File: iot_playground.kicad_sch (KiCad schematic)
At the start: 34 parts, among them J101 Micro_SD_Card_Det_Hirose_DM3C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, J102 Conn_01x02, J104 Conn_01x04, J105 Conn_01x04, J701 Conn_01x08, SW101 SW_SPST, SW102 SW_SPST, U101 ESP32-WROOM-32D, U102 LTR-F216A, U103 UHE4913, U104 LIS2DW12

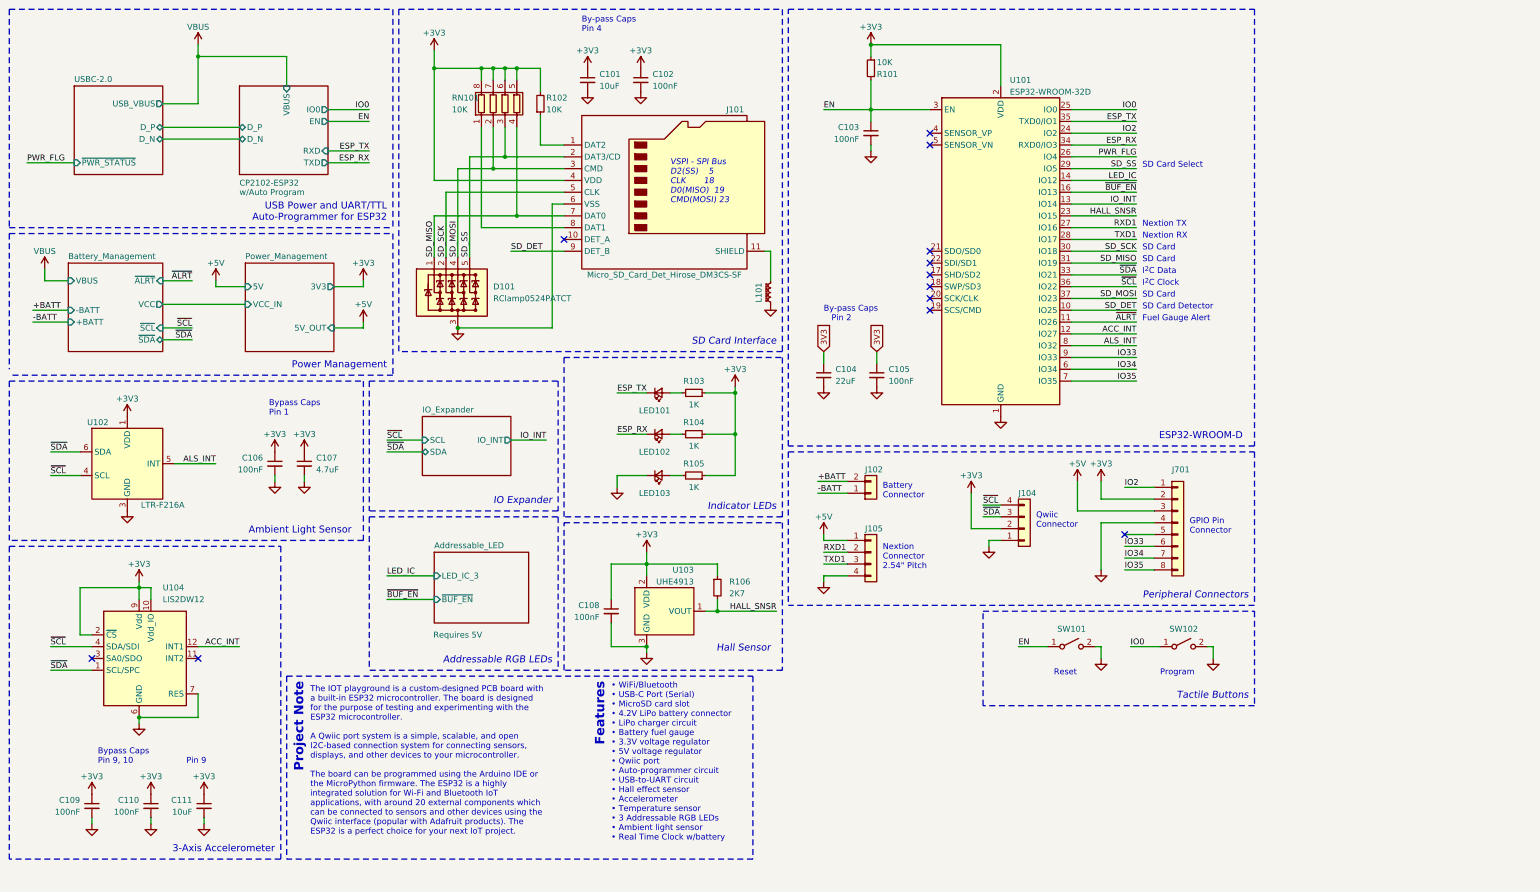
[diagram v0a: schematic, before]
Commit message: add RTC, humidity and temp sensors
updated footprint paths
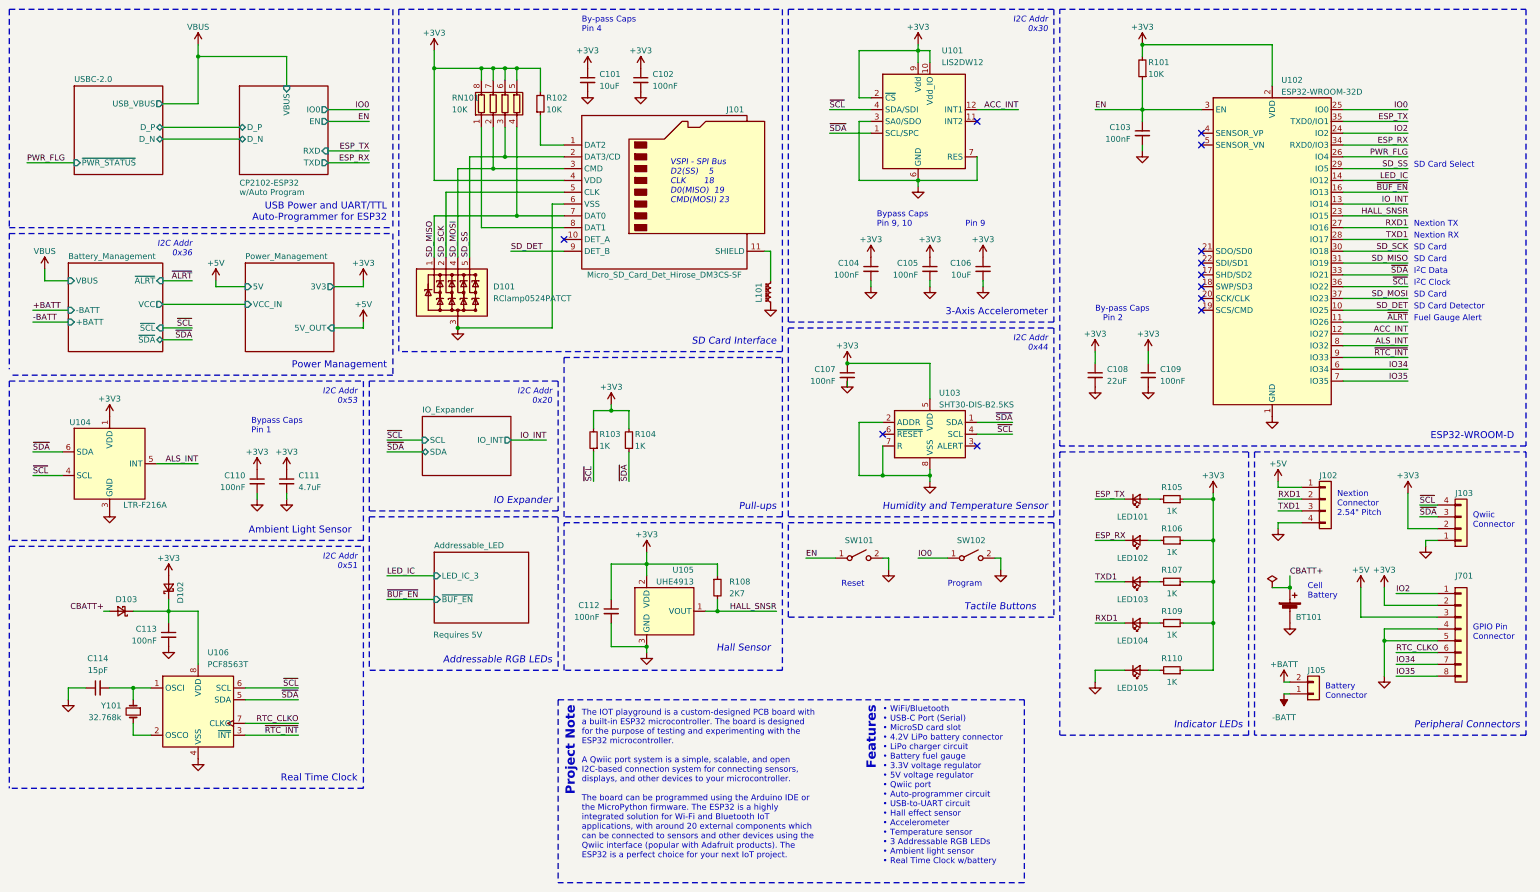
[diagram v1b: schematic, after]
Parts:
- added BT101: Battery_Cell, User Custom Footprint:BatteryHolder_CR1220, symbol Device:Battery_Cell
- added C107: 100nF, Capacitor_SMD:C_0603_1608Metric, symbol Device:C_Small
- added C113: 100nF, Capacitor_SMD:C_0805_2012Metric, symbol Device:C_Small
- added C114: 15pF, Capacitor_SMD:C_0603_1608Metric, symbol Device:C_Small
- added D102, D103: D_Schottky, Diode_SMD:D_SMA, symbol Device:D_Schottky_Small
- added LED103: BLUE, LED_SMD:LED_0603_1608Metric, symbol Device:LED_Small
- added LED104: GREEN, LED_SMD:LED_0603_1608Metric, symbol Device:LED_Small
- added R103, R104, R107, R109: 1K, Resistor_SMD:R_0603_1608Metric, symbol Device:R_Small
- added U103: SHT30-DIS-B2.5KS, Sensor_Humidity:Sensirion_DFN-8-1EP_2.5x2.5mm_P0.5mm_EP1.1x1.7mm, symbol Sensor_Humidity:SHT30-DIS
- added U106: PCF8563T, Package_SO:SOIC-8_3.9x4.9mm_P1.27mm, symbol Timer_RTC:PCF8563T
- added Y101: 32.768k, Crystal:Crystal_SMD_3215-2Pin_3.2x1.5mm, symbol Device:Crystal_Small
- renumbered C109 to C104, C110 to C105, C111 to C106, C104 to C108, C105 to C109, C106 to C110, C107 to C111, C108 to C112, J105 to J102, J104 to J103, J102 to J105, LED103 to LED105, R103 to R105, R104 to R106, R106 to R108, R105 to R110, U104 to U101, U101 to U102, U102 to U104, U103 to U105
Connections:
- net 3V3 is gone; now on net +3V3: C108.1, C109.1
- net +3V3: now also R101.2, C107.1, D102.2 (A), R103.2, R104.2, R107.1, R109.1, U103.5 (VDD); no longer R101.1
- net EN: now also R101.1; no longer R101.2
- net GND: now also J701.5 (Pin_5), U101.3 (SA0/SDO), BT101.2 (-), C107.2, C113.2, C114.1, U103.2 (ADDR), U103.7 (R), U103.8 (VSS), U103.9 (VSS), U106.4 (VSS)
- net RXD1: now also LED104.1 (K)
- net TXD1: now also LED103.1 (K)
- net ~{SCL}: now also R103.1, U103.4 (SCL), U106.6 (SCL)
- net ~{SDA}: now also R104.1, U103.1 (SDA), U106.5 (SDA)
- net IO33 renamed RTC_CLKO
- net RTC_CLKO: now also U106.7 (CLKO); no longer U102.9 (IO33)
- new net: C113.1, D102.1 (K), D103.1 (K), U106.8 (VDD)
- new net: C114.2, U106.1 (OSCI), Y101.1
- new net: U106.2 (OSCO), Y101.2
- new net: LED103.2 (A), R107.2
- new net: LED104.2 (A), R109.2
- new net CBATT+: BT101.1 (+), D103.2 (A)
- new net ~{RTC_INT}: U102.9 (IO33), U106.3 (~{INT})
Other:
- note added: "Cell Battery"
- note added: "Humidity and Temperature Sensor"
- note added: "I2C Addr 0x20"
- note added: "I2C Addr 0x30"
- note added: "I2C Addr 0x36"
- note added: "I2C Addr 0x44"
- note added: "I2C Addr 0x51"
- note added: "I2C Addr 0x53"
- note added: "Pull-ups"
- note added: "Real Time Clock"
- moved on the sheet: C103, C104, C105, C106, C108, C109, C110, C111, J102, J103, J105, J701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

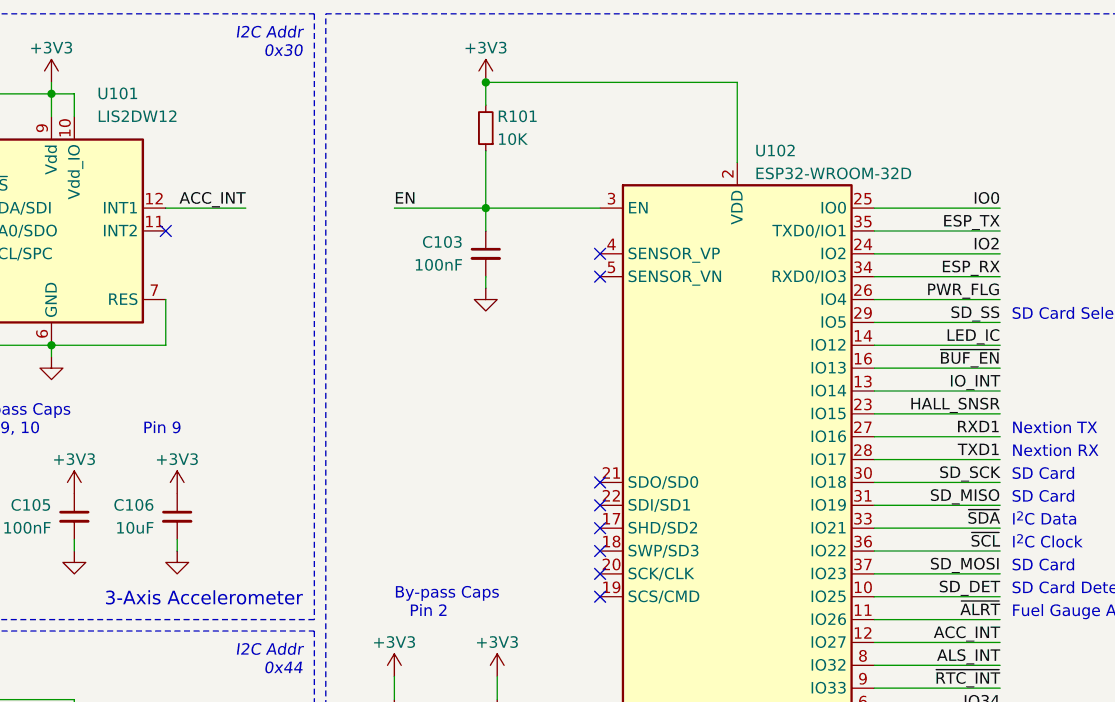
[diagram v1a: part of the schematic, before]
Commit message: update LCSC parts and footprints
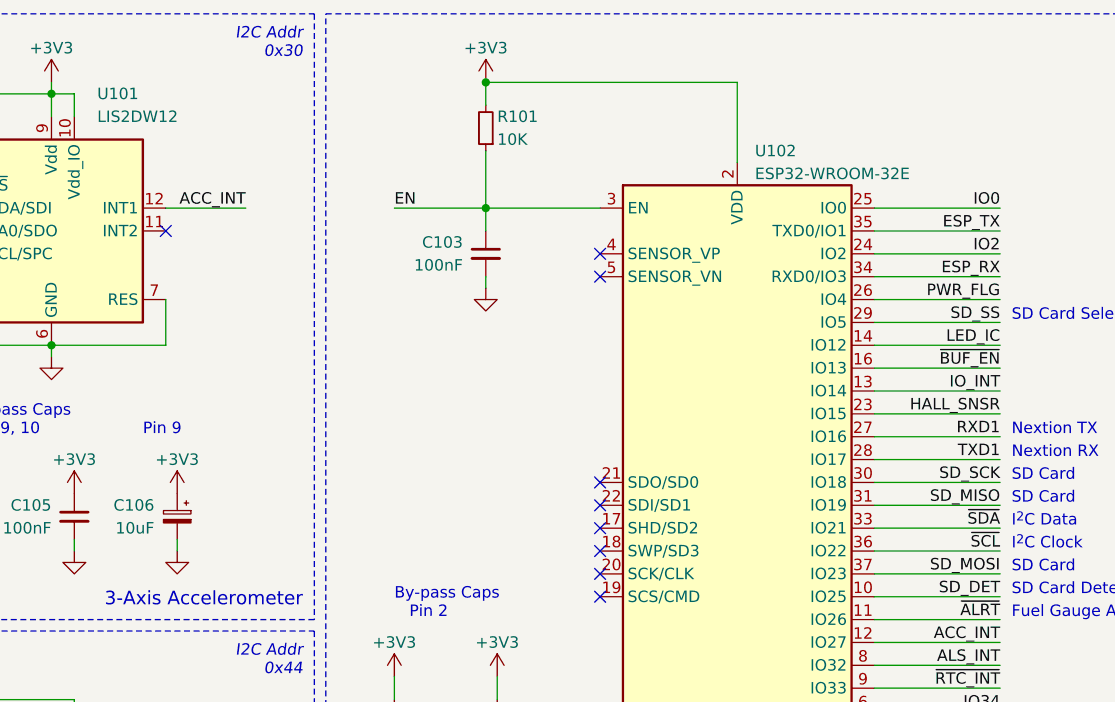
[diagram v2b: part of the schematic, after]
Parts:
- C106: footprint Capacitor_SMD:C_0603_1608Metric -> Capacitor_SMD:CP_Elec_5x5.4; symbol Device:C_Small -> Device:C_Polarized_Small; LCSC (none) -> C335978
- J102: footprint (none) -> Connector_PinHeader_2.54mm:PinHeader_1x04_P2.54mm_Vertical
- J103: footprint (none) -> Connector_JST:JST_SH_BM04B-SRSS-TB_1x04-1MP_P1.00mm_Vertical
- R103, R104: LCSC (none) -> C21190
- U102: value ESP32-WROOM-32D -> ESP32-WROOM-32E; LCSC (none) -> C701341
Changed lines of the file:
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@@
       (effects (font (size 1.27 1.27)) hide)
     )
-    (property "LCSC" "" (at 140.97 106.68 0)
+    (property "LCSC" "C21190" (at 140.97 106.68 0)
       (effects (font (size 1.27 1.27)) hide)
     )
@@
       (effects (font (size 1.27 1.27)) (justify left) hide)
     )
-    (property "Footprint" "" (at 327.66 125.73 0)
+    (property "Footprint" "Connector_JST:JST_SH_BM04B-SRSS-TB_1x04-1MP_P1.00mm_Vertical" (at 327.66 125.73 0)
       (effects (font (size 1.27 1.27)) hide)
     )
@@
       (effects (font (size 1.27 1.27)) (justify left) hide)
     )
-    (property "Footprint" "" (at 298.45 119.38 0)
+    (property "Footprint" "Connector_PinHeader_2.54mm:PinHeader_1x04_P2.54mm_Vertical" (at 298.45 119.38 0)
       (effects (font (size 1.27 1.27)) hide)
     )
@@
       (effects (font (size 1.27 1.27)) (justify left))
     )
-    (property "Value" "ESP32-WROOM-32D" (at 288.9759 31.75 0)
+    (property "Value" "ESP32-WROOM-32E" (at 288.9759 31.75 0)
       (effects (font (size 1.27 1.27)) (justify left))
     )
@@
     )
     (property "Datasheet" "https://www.espressif.com/sites/default/files/documentation/esp32-wroom-32d_esp32-wroom-32u_datasheet_en.pdf" (at 279.4 64.77 0)
+      (effects (font (size 1.27 1.27)) hide)
+    )
+    (property "LCSC" "C701341" (at 287.02 66.04 0)
       (effects (font (size 1.27 1.27)) hide)
     )
@@
       (effects (font (size 1.27 1.27)) hide)
     )
-    (property "LCSC" "" (at 148.59 106.68 0)
+    (property "LCSC" "C21190" (at 148.59 106.68 0)
       (effects (font (size 1.27 1.27)) hide)
     )
@@
     )
   )
-  (symbol (lib_id "Device:C_Small") (at 224.79 69.85 0) (mirror y) (unit 1)
+  (symbol (lib_id "Device:C_Polarized_Small") (at 224.79 69.85 0) (mirror y) (unit 1)
     (in_bom yes) (on_board yes) (dnp no)
     (property "Reference" "C106" (at 222.25 68.5862 0)
@@
       (effects (font (size 1.27 1.27)) (justify left))
     )
-    (property "Footprint" "Capacitor_SMD:C_0603_1608Metric" (at 224.79 69.85 0)
+    (property "Footprint" "Capacitor_SMD:CP_Elec_5x5.4" (at 224.79 69.85 0)
       (effects (font (size 1.27 1.27)) hide)
     )
@@
       (effects (font (size 1.27 1.27)) hide)
     )
-    (property "LCSC" "" (at 224.79 69.85 0)
-      (effects (font (size 1.27 1.27)) hide)
-    )
+    (property "LCSC" "C335978" (at 224.79 69.85 0)
+      (effects (font (size 1.27 1.27)) hide)
+    )

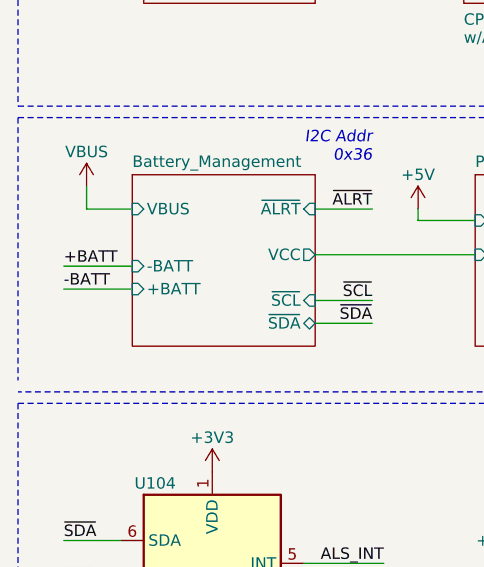
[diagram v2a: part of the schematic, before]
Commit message: update 3d models
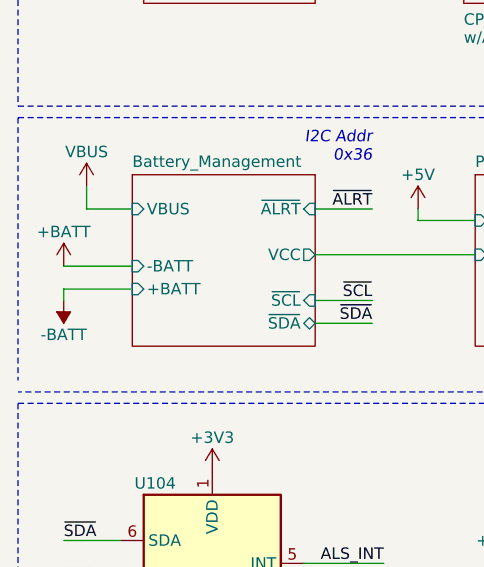
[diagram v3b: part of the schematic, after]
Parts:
- J103: footprint Connector_JST:JST_SH_BM04B-SRSS-TB_1x04-1MP_P1.00mm_Vertical -> Connector_JST:JST_SH_SM04B-SRSS-TB_1x04-1MP_P1.00mm_Horizontal
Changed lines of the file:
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@@
     (stroke (width 0) (type default))
   )
-  (wire (pts (xy 20.32 81.28) (xy 27.94 81.28))
-    (stroke (width 0) (type default))
-  )
   (wire (pts (xy 259.08 43.18) (xy 259.08 44.45))
     (stroke (width 0) (type default))
@@
     (stroke (width 0) (type default))
   )
+  (wire (pts (xy 20.32 81.28) (xy 27.94 81.28))
+    (stroke (width 0) (type default))
+  )
   (wire (pts (xy 311.15 142.24) (xy 322.58 142.24))
     (stroke (width 0) (type default))
@@
     (stroke (width 0) (type default))
   )
+  (wire (pts (xy 20.32 81.28) (xy 20.32 82.55))
+    (stroke (width 0) (type default))
+  )
   (wire (pts (xy 111.76 48.26) (xy 111.76 67.31))
     (stroke (width 0) (type default))
@@
     (effects (font (size 1.27 1.27)) (justify right bottom))
   )
-  (label "-BATT" (at 20.32 81.28 0) (fields_autoplaced)
-    (effects (font (size 1.27 1.27)) (justify left bottom))
-  )
   (label "TXD1" (at 316.23 63.5 180) (fields_autoplaced)
     (effects (font (size 1.27 1.27)) (justify right bottom))
@@
     (effects (font (size 1.27 1.27)) (justify left bottom))
   )
-  (label "+BATT" (at 20.32 78.74 0) (fields_autoplaced)
-    (effects (font (size 1.27 1.27)) (justify left bottom))
-  )
   (label "RTC_CLKO" (at 77.47 167.64 180) (fields_autoplaced)
     (effects (font (size 1.27 1.27)) (justify right bottom))
@@
       (effects (font (size 1.27 1.27)) (justify left) hide)
     )
-    (property "Footprint" "Connector_JST:JST_SH_BM04B-SRSS-TB_1x04-1MP_P1.00mm_Vertical" (at 327.66 125.73 0)
+    (property "Footprint" "Connector_JST:JST_SH_SM04B-SRSS-TB_1x04-1MP_P1.00mm_Horizontal" (at 327.66 125.73 0)
       (effects (font (size 1.27 1.27)) hide)
     )
@@
       (effects (font (size 1.27 1.27)) hide)
     )
+    (property "LCSC" "" (at 327.66 125.73 0)
+      (effects (font (size 1.27 1.27)) hide)
+    )
     (pin "1")
     (pin "2")
@@
     )
   )
+  (symbol (lib_id "power:-BATT") (at 20.32 82.55 180) (unit 1)
+    (in_bom yes) (on_board yes) (dnp no)
+    (property "Reference" "#PWR0159" (at 20.32 78.74 0)
+      (effects (font (size 1.27 1.27)) hide)
+    )
+    (property "Value" "-BATT" (at 20.32 86.36 0)
+      (effects (font (size 1.27 1.27)))
+    )
+    (property "Footprint" "" (at 20.32 82.55 0)
+      (effects (font (size 1.27 1.27)) hide)
+    )
+    (property "Datasheet" "" (at 20.32 82.55 0)
+      (effects (font (size 1.27 1.27)) hide)
+    )
+    (pin "1")
+    (instances
+      (project "iot_playground"
+        (path "/da21b043-c1be-47f1-86d6-d54e7594fd6d"
+          (reference "#PWR0159") (unit 1)
+        )
+      )
+    )
+  )
   (symbol (lib_id "power:+3V3") (at 210.82 21.59 0) (unit 1)
     (in_bom yes) (on_board yes) (dnp no)
@@
         )
       )
+    )
+  )
+  (symbol (lib_id "power:+BATT") (at 20.32 78.74 0) (unit 1)
+    (in_bom yes) (on_board yes) (dnp no) (fields_autoplaced)
+    (property "Reference" "#PWR0158" (at 20.32 82.55 0)
+      (effects (font (size 1.27 1.27)) hide)
+    )
+    (property "Value" "+BATT" (at 20.32 74.93 0)
+      (effects (font (size 1.27 1.27)))
+    )
+    (property "Footprint" "" (at 20.32 78.74 0)
+      (effects (font (size 1.27 1.27)) hide)
+    )
+    (property "Datasheet" "" (at 20.32 78.74 0)
+      (effects (font (size 1.27 1.27)) hide)
+    )
+    (pin "1")
+    (instances
+      (project "iot_playground"
+        (path "/da21b043-c1be-47f1-86d6-d54e7594fd6d"
+          (reference "#PWR0158") (unit 1)
+        )
+      )
